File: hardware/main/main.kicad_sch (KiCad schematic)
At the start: 28 parts, among them J101 ST_LINK, J102 USART

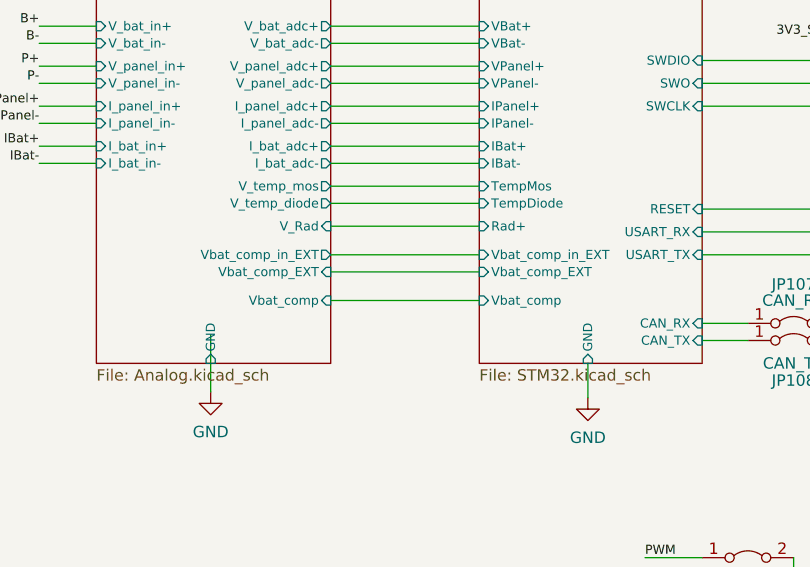
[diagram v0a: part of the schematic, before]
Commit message: Layout: Organize and initialize routing of control
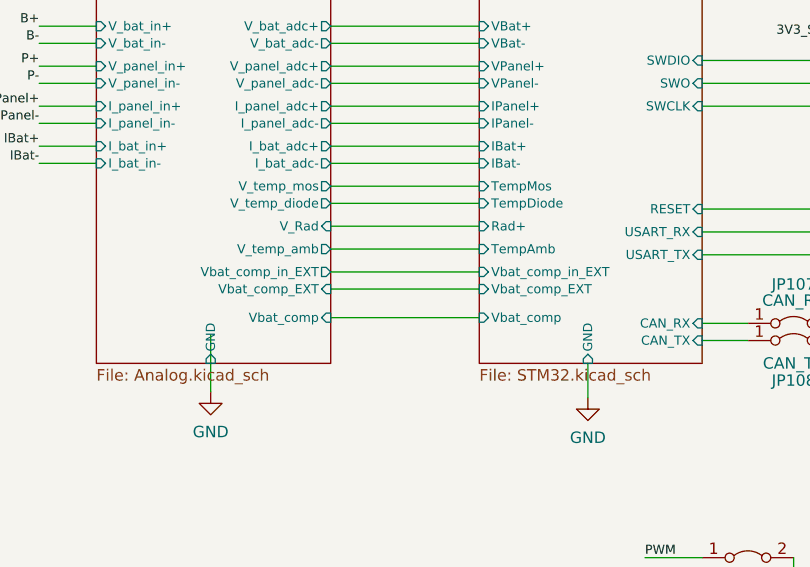
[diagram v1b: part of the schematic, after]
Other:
- sheet Analog ports: added V_temp_amb; removed none
- sheet STM32 ports: added TempAmb; removed none

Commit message: Layout: Connect all unconected nets, and fix all DRC errors
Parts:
- JP101, JP102, JP103, JP104, JP105, JP106, JP107, JP108, JP109, JP110: footprint Zenite:SolderJumper-2_P0.5mm_Open_TrianglePad0.5x0.5mm -> Zenite:SolderJumper-2_P0.5mm_Open_TrianglePad0.8x0.5mm

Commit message: Layout: Silkscreen updated
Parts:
- added LOGO103: Logo_Open_Hardware_Small, Symbol:OSHW-Logo_5.7x6mm_SilkScreen, symbol Graphic:Logo_Open_Hardware_Small
- added LOGO104: Logo_Open_Hardware_Small, Zenite:symbol_logoZenite_small, symbol Graphic:Logo_Open_Hardware_Small
- added LOGO105: (no value), symbol Graphic:Logo_Open_Hardware_Small
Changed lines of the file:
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@@
     (effects (font (size 1.016 1.016)) (justify left bottom))
+  )
+  (symbol (lib_id "Graphic:Logo_Open_Hardware_Small") (at 41.275 188.595 0) (unit 1)
+    (in_bom yes) (on_board yes) (fields_autoplaced)
+    (property "Reference" "LOGO104" (id 0) (at 41.275 181.61 0)
+      (effects (font (size 1.27 1.27)) hide)
+    )
+    (property "Value" "Logo_Open_Hardware_Small" (id 1) (at 41.275 194.31 0)
+      (effects (font (size 1.27 1.27)) hide)
+    )
+    (property "Footprint" "Zenite:symbol_logoZenite_small" (id 2) (at 41.275 188.595 0)
+      (effects (font (size 1.27 1.27)) hide)
+    )
+    (property "Datasheet" "~" (id 3) (at 41.275 188.595 0)
+      (effects (font (size 1.27 1.27)) hide)
+    )
   )
   (symbol (lib_id "Device:NetTie_2") (at 130.175 125.095 90) (mirror x) (unit 1)
@@
     (pin "1")
     (pin "2")
+  )
+  (symbol (lib_id "Graphic:Logo_Open_Hardware_Small") (at 55.245 188.595 0) (unit 1)
+    (in_bom yes) (on_board yes) (fields_autoplaced)
+    (property "Reference" "LOGO105" (id 0) (at 55.245 181.61 0)
+      (effects (font (size 1.27 1.27)) hide)
+    )
+    (property "Value" "" (id 1) (at 55.245 194.31 0)
+      (effects (font (size 1.27 1.27)) hide)
+    )
+    (property "Footprint" "" (id 2) (at 55.245 188.595 0)
+      (effects (font (size 1.27 1.27)) hide)
+    )
+    (property "Datasheet" "~" (id 3) (at 55.245 188.595 0)
+      (effects (font (size 1.27 1.27)) hide)
+    )
   )
   (symbol (lib_id "Device:R") (at 135.89 127.635 90) (mirror x) (unit 1)
@@
     (pin "1")
     (pin "2")
+  )
+  (symbol (lib_id "Graphic:Logo_Open_Hardware_Small") (at 27.305 187.96 0) (unit 1)
+    (in_bom yes) (on_board yes) (fields_autoplaced)
+    (property "Reference" "LOGO103" (id 0) (at 27.305 180.975 0)
+      (effects (font (size 1.27 1.27)) hide)
+    )
+    (property "Value" "Logo_Open_Hardware_Small" (id 1) (at 27.305 193.675 0)
+      (effects (font (size 1.27 1.27)) hide)
+    )
+    (property "Footprint" "Symbol:OSHW-Logo_5.7x6mm_SilkScreen" (id 2) (at 27.305 187.96 0)
+      (effects (font (size 1.27 1.27)) hide)
+    )
+    (property "Datasheet" "~" (id 3) (at 27.305 187.96 0)
+      (effects (font (size 1.27 1.27)) hide)
+    )
   )
   (symbol (lib_id "Jumper:Jumper_2_Bridged") (at 166.37 88.265 0) (unit 1)
@@
       (reference "LOGO102") (unit 1) (value "Logo_Open_Hardware_Small") (footprint "Zenite:synbol_logoifsc")
     )
+    (path "/9d04926f-36c0-4fcd-b151-69a639110201"
+      (reference "LOGO103") (unit 1) (value "Logo_Open_Hardware_Small") (footprint "Symbol:OSHW-Logo_5.7x6mm_SilkScreen")
+    )
+    (path "/0975f659-a5ca-41b7-b49e-2ece00ca09b7"
+      (reference "LOGO104") (unit 1) (value "Logo_Open_Hardware_Small") (footprint "Zenite:symbol_logoZenite_small")
+    )
+    (path "/1bde768f-9ae6-4a6b-91a2-b38c732d0f79"
+      (reference "LOGO105") (unit 1) (value "Logo_Open_Hardware_Small") (footprint "Zenite:synbol_logoifsc_small")
+    )
     (path "/9e3280d3-dce3-416e-a0bb-0596067104fa/83f954fe-32e5-4f24-9b2a-ba7cfd1adb03"

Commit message: layout: Separating analogical power nets
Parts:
- added D103, D104, D105, D106, D107, D108: ESD351DPYR, Diode_SMD:D_0402_1005Metric_Pad0.77x0.64mm_HandSolder, symbol Device:D_TVS
- LOGO105: value (none) -> Logo_Open_Hardware_Small; footprint (none) -> Zenite:synbol_logoifsc_small
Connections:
- net GND: now also D103.1 (A1), D104.1 (A1), D105.1 (A1), D106.1 (A1), D107.1 (A1), D108.1 (A1)
- net STM32/RESET renamed RESET
- net RESET: now also D106.2 (A2)
- net STM32/SWCLK renamed SWCLK
- net SWCLK: now also D105.2 (A2)
- net STM32/SWDIO renamed SWDIO
- net SWDIO: now also D103.2 (A2)
- net STM32/SWO renamed SWO
- net SWO: now also D104.2 (A2)
- net STM32/USART_RX renamed USART_RX
- net USART_RX: now also D107.2 (A2)
- net STM32/USART_TX renamed USART_TX
- net USART_TX: now also D108.2 (A2)
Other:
- sheet Analog ports: added 3V3A; removed 3V3
